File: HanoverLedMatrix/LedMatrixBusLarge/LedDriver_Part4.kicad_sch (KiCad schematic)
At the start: 200 parts

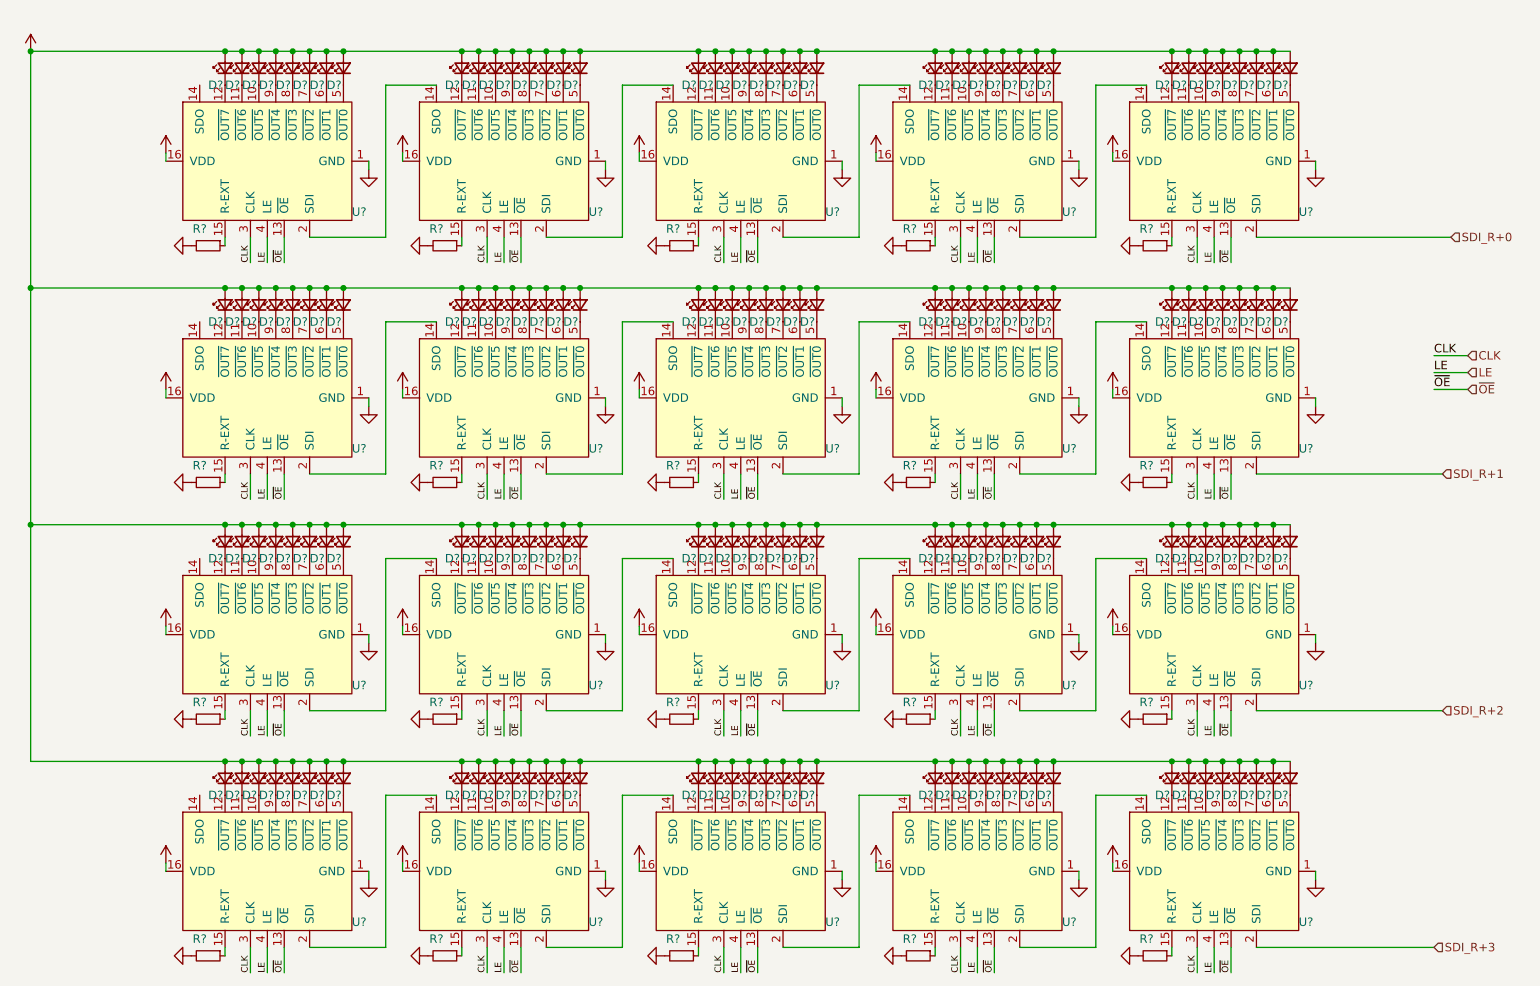
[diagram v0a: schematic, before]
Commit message: feat: Updated the symbol of 74HC373D
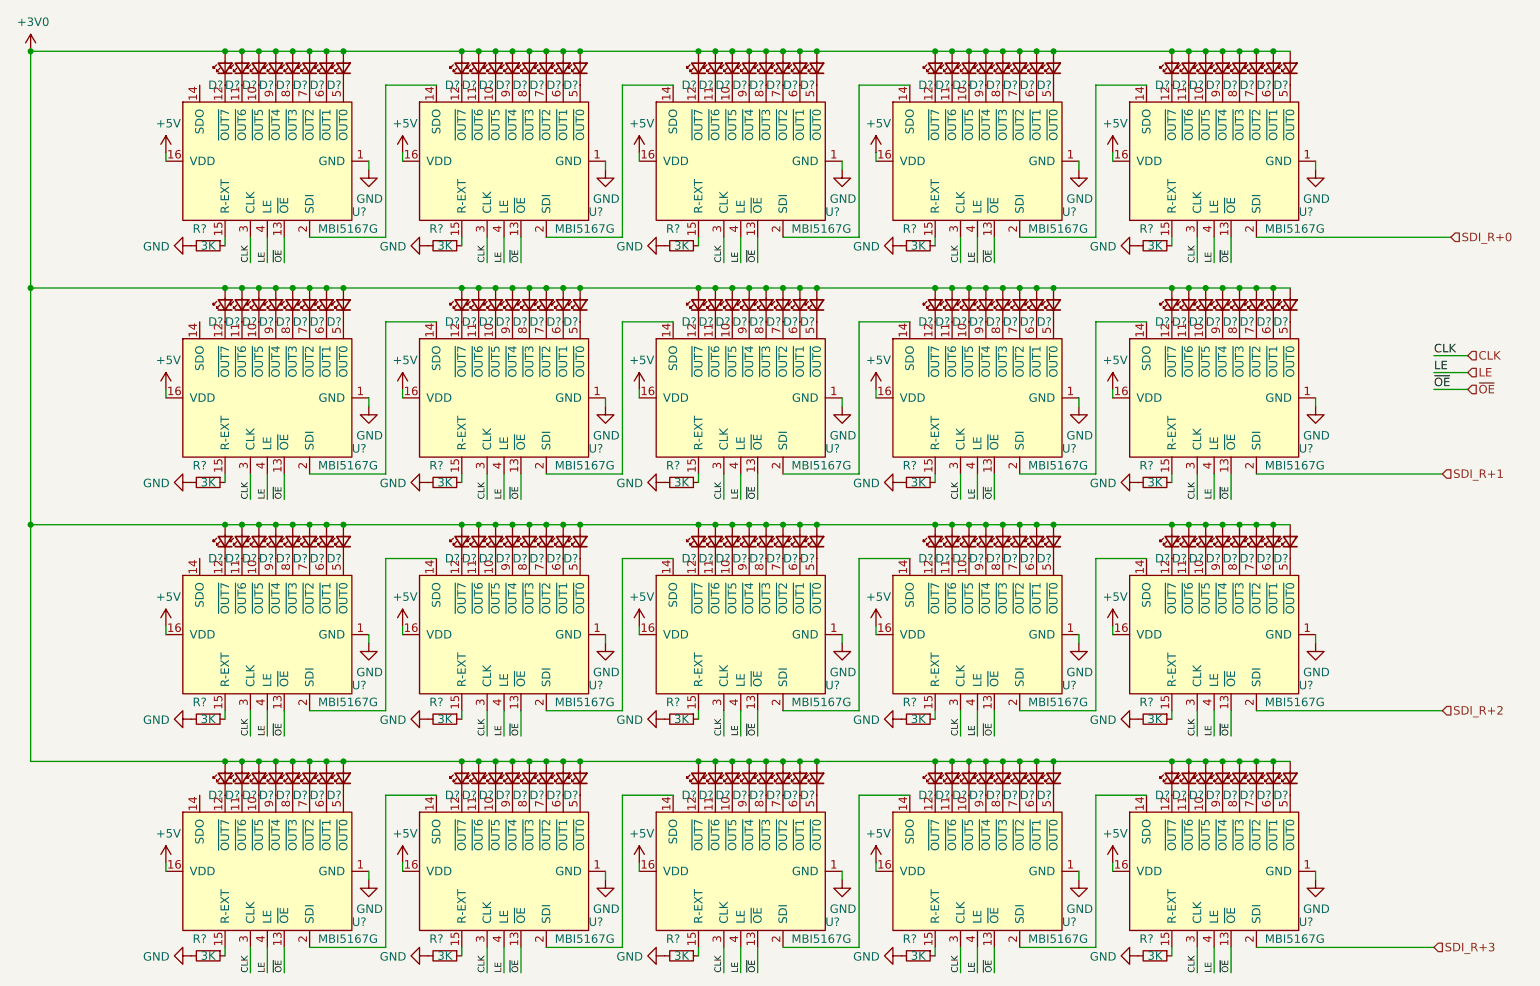
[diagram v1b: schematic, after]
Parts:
- D? (x160): value (none) -> LED_Small
- R? (x20): value (none) -> 3K
- U? (x20): value (none) -> MBI5167G

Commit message: feat: organised the schematic into blocks and updated the readme
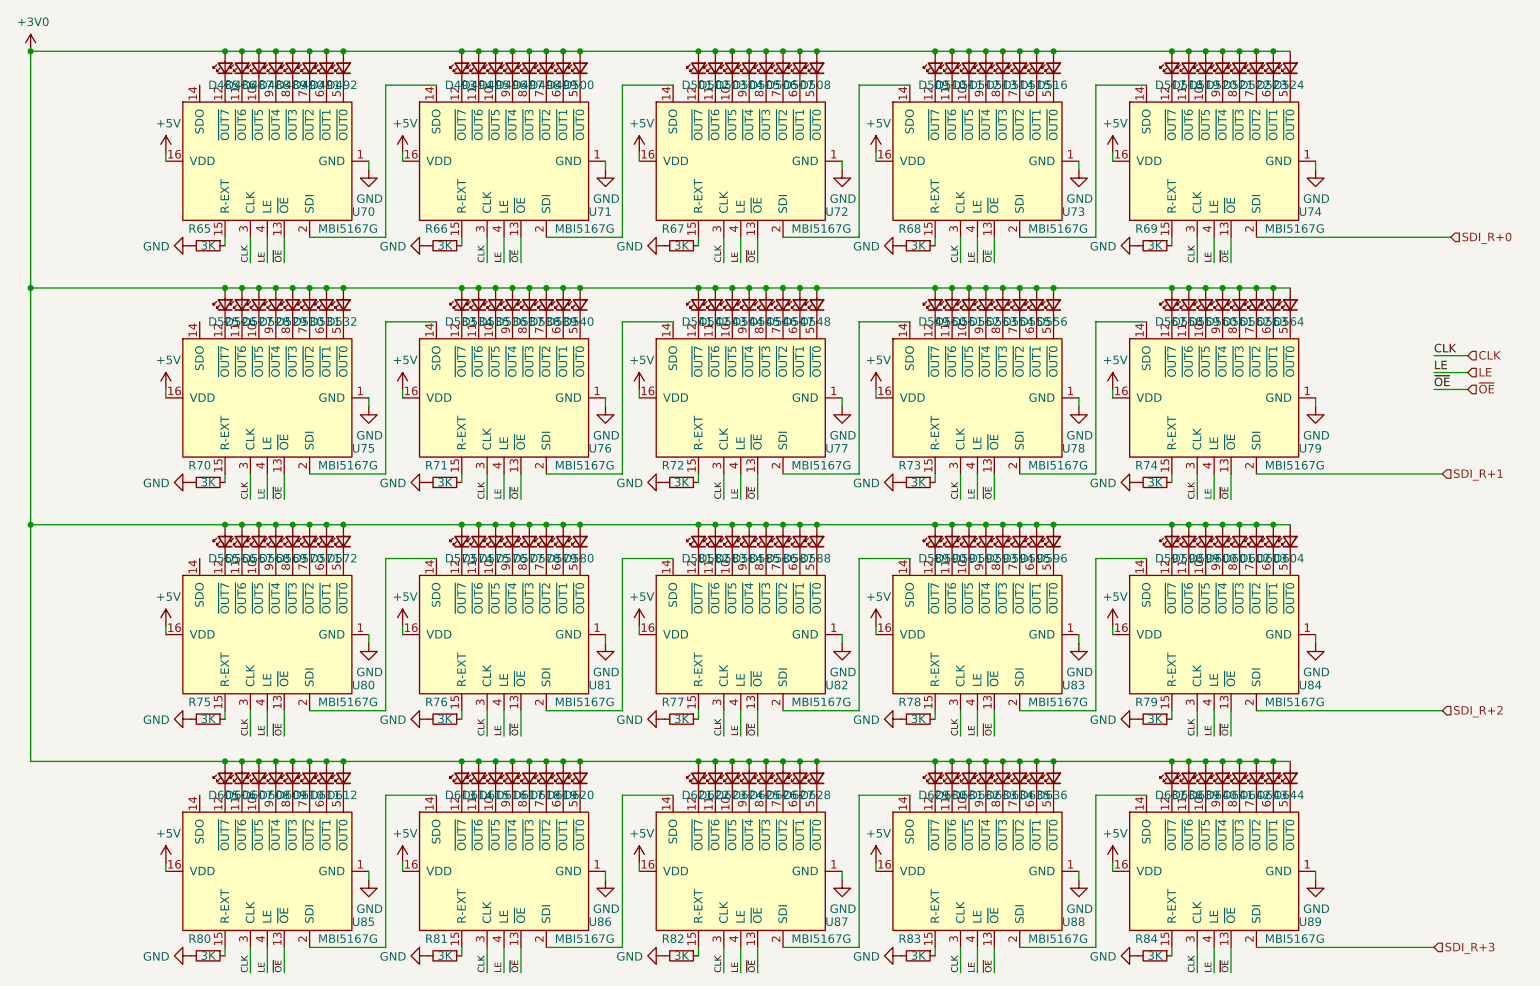
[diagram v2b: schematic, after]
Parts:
- gave numbers to parts that had none: 200
